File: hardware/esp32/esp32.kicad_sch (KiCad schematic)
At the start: 61 parts, among them J1 Screw_Terminal_01x02, J2 ESP_left, J3 ESP_right, Q4 MMBT5401, Q5 MMBT2222A, U5 LMV321, U6 LM393, U6 LMV321, U8 HT7533-1

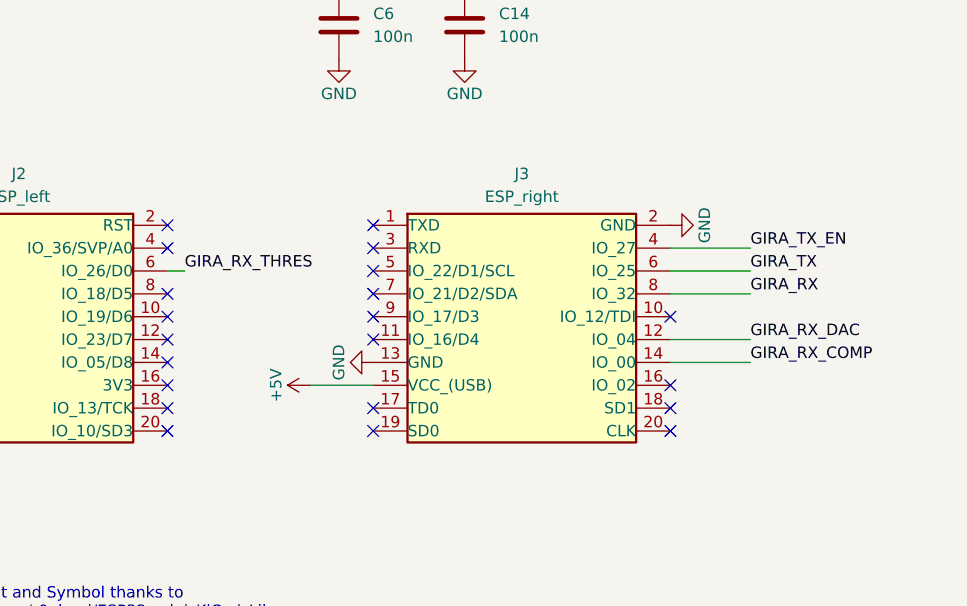
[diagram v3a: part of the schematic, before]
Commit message: Mark boot pins and move rx pins to non boot pins
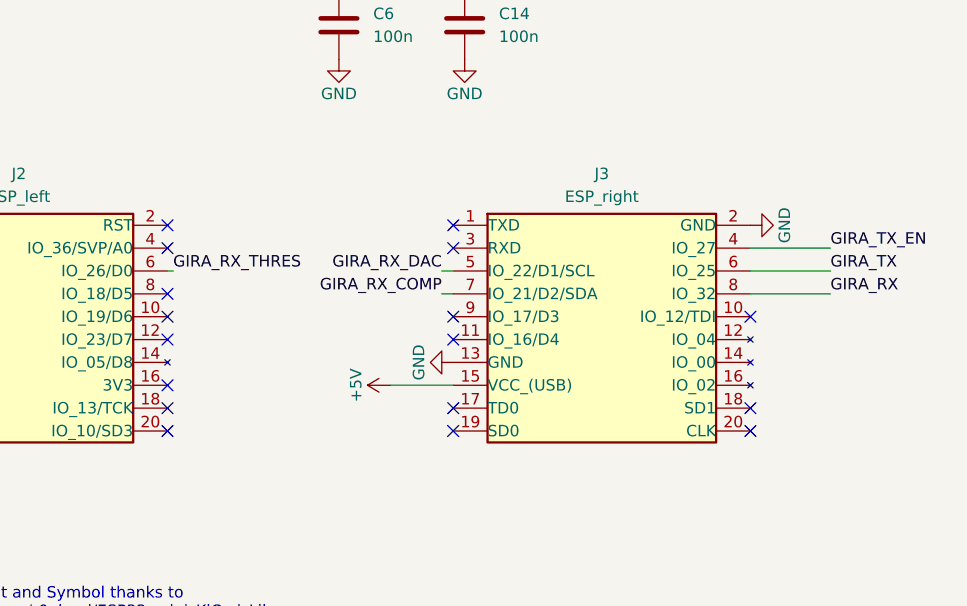
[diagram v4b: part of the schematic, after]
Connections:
- net GIRA_RX_COMP: now also J3.7 (IO_21/D2/SDA); no longer J3.14 (IO_00)
- net GIRA_RX_DAC: now also J3.5 (IO_22/D1/SCL); no longer J3.12 (IO_04)
- no-connect marks 30 -> 26
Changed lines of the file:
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@@
   (no_connect (at 320.04 112.395))
   (no_connect (at 287.02 114.935))
-  (no_connect (at 375.92 117.475))
   (no_connect (at 320.04 109.855))
-  (no_connect (at 342.9 102.235))
+  (no_connect (at 351.79 102.235))
   (no_connect (at 287.02 112.395))
   (no_connect (at 287.02 102.235))
-  (no_connect (at 342.9 122.555))
+  (no_connect (at 351.79 122.555))
   (no_connect (at 287.02 107.315))
   (no_connect (at 287.02 109.855))
@@
   (no_connect (at 320.04 99.695))
   (no_connect (at 320.04 117.475))
-  (no_connect (at 342.9 112.395))
-  (no_connect (at 342.9 109.855))
+  (no_connect (at 351.79 112.395))
+  (no_connect (at 351.79 109.855))
   (no_connect (at 287.02 120.015))
-  (no_connect (at 320.04 114.935))
   (no_connect (at 287.02 122.555))
-  (no_connect (at 342.9 107.315))
-  (no_connect (at 342.9 120.015))
+  (no_connect (at 351.79 120.015))
   (no_connect (at 320.04 122.555))
   (no_connect (at 320.04 120.015))
   (no_connect (at 287.02 104.775))
-  (no_connect (at 375.92 120.015))
-  (no_connect (at 375.92 122.555))
-  (no_connect (at 375.92 109.855))
-  (no_connect (at 342.9 99.695))
+  (no_connect (at 384.81 120.015))
+  (no_connect (at 384.81 122.555))
+  (no_connect (at 384.81 109.855))
+  (no_connect (at 351.79 99.695))
   (no_connect (at 287.02 117.475))
   (no_connect (at 320.04 102.235))
-  (no_connect (at 342.9 104.775))
   (wire (pts (xy 235.585 231.14) (xy 235.585 232.41))
     (stroke (width 0) (type default))
@@
     (stroke (width 0) (type default))
   )
-  (wire (pts (xy 384.81 104.775) (xy 375.92 104.775))
+  (wire (pts (xy 393.7 104.775) (xy 384.81 104.775))
     (stroke (width 0) (type default))
   )
@@
     (stroke (width 0) (type default))
   )
-  (wire (pts (xy 335.915 117.475) (xy 342.9 117.475))
+  (wire (pts (xy 344.805 117.475) (xy 351.79 117.475))
     (stroke (width 0) (type default))
   )
@@
     (stroke (width 0) (type default))
   )
-  (wire (pts (xy 375.92 107.315) (xy 384.81 107.315))
+  (wire (pts (xy 384.81 107.315) (xy 393.7 107.315))
     (stroke (width 0) (type default))
   )
@@
     (stroke (width 0) (type default))
   )
-  (wire (pts (xy 384.81 102.235) (xy 375.92 102.235))
+  (wire (pts (xy 393.7 102.235) (xy 384.81 102.235))
     (stroke (width 0) (type default))
   )
@@
     (stroke (width 0) (type default))
   )
-  (wire (pts (xy 321.945 104.775) (xy 320.04 104.775))
+  (wire (pts (xy 320.675 104.775) (xy 320.04 104.775))
     (stroke (width 0) (type default))
   )
@@
     (stroke (width 0) (type default))
   )
-  (wire (pts (xy 384.81 114.935) (xy 375.92 114.935))
+  (wire (pts (xy 350.52 107.315) (xy 351.79 107.315))
     (stroke (width 0) (type default))
   )
-  (wire (pts (xy 384.81 112.395) (xy 375.92 112.395))
+  (wire (pts (xy 350.52 104.775) (xy 351.79 104.775))
     (stroke (width 0) (type default))
   )
@@
     (effects (font (size 1.27 1.27)) (justify left bottom))
   )
-  (label "GIRA_RX_DAC" (at 384.81 112.395 0) (fields_autoplaced)
-    (effects (font (size 1.27 1.27)) (justify left bottom))
+  (label "GIRA_RX_DAC" (at 350.52 104.775 180) (fields_autoplaced)
+    (effects (font (size 1.27 1.27)) (justify right bottom))
   )
   (label "GIRA_RX" (at 257.81 53.34 0) (fields_autoplaced)
@@
     (effects (font (size 1.27 1.27)) (justify right bottom))
   )
-  (label "GIRA_RX_COMP" (at 384.81 114.935 0) (fields_autoplaced)
-    (effects (font (size 1.27 1.27)) (justify left bottom))
+  (label "GIRA_RX_COMP" (at 350.52 107.315 180) (fields_autoplaced)
+    (effects (font (size 1.27 1.27)) (justify right bottom))
   )
   (label "GIRA_TX_EN" (at 266.065 178.435 180) (fields_autoplaced)
     (effects (font (size 1.27 1.27)) (justify right bottom))
   )
-  (label "GIRA_RX_THRES" (at 321.945 104.775 0) (fields_autoplaced)
+  (label "GIRA_RX_THRES" (at 320.675 104.775 0) (fields_autoplaced)
     (effects (font (size 1.27 1.27)) (justify left bottom))
   )
-  (label "GIRA_RX" (at 384.81 107.315 0) (fields_autoplaced)
+  (label "GIRA_RX" (at 393.7 107.315 0) (fields_autoplaced)
     (effects (font (size 1.27 1.27)) (justify left bottom))
   )
-  (label "GIRA_TX_EN" (at 384.81 102.235 0) (fields_autoplaced)
+  (label "GIRA_TX_EN" (at 393.7 102.235 0) (fields_autoplaced)
     (effects (font (size 1.27 1.27)) (justify left bottom))
   )
-  (label "GIRA_TX" (at 384.81 104.775 0) (fields_autoplaced)
+  (label "GIRA_TX" (at 393.7 104.775 0) (fields_autoplaced)
     (effects (font (size 1.27 1.27)) (justify left bottom))
   )
@@
     )
   )
-  (symbol (lib_id "symbols:GND") (at 342.9 114.935 270) (mirror x) (unit 1)
+  (symbol (lib_id "symbols:GND") (at 351.79 114.935 270) (mirror x) (unit 1)
     (in_bom yes) (on_board yes) (dnp no)
-    (property "Reference" "#PWR0120" (at 336.55 114.935 0)
+    (property "Reference" "#PWR0120" (at 345.44 114.935 0)
       (effects (font (size 1.27 1.27)) hide)
     )
-    (property "Value" "GND" (at 339.09 114.935 0)
+    (property "Value" "GND" (at 347.98 114.935 0)
       (effects (font (size 1.27 1.27)))
     )
-    (property "Footprint" "" (at 342.9 114.935 0)
+    (property "Footprint" "" (at 351.79 114.935 0)
       (effects (font (size 1.27 1.27)) hide)
     )
-    (property "Datasheet" "" (at 342.9 114.935 0)
+    (property "Datasheet" "" (at 351.79 114.935 0)
       (effects (font (size 1.27 1.27)) hide)
     )
@@
     )
   )
-  (symbol (lib_id "symbols:ESP_right") (at 347.98 109.855 0) (unit 1)
+  (symbol (lib_id "symbols:ESP_right") (at 356.87 109.855 0) (unit 1)
     (in_bom yes) (on_board yes) (dnp no) (fields_autoplaced)
-    (property "Reference" "J3" (at 359.41 93.98 0)
+    (property "Reference" "J3" (at 368.3 93.98 0)
       (effects (font (size 1.27 1.27)))
     )
-    (property "Value" "ESP_right" (at 359.41 96.52 0)
+    (property "Value" "ESP_right" (at 368.3 96.52 0)
       (effects (font (size 1.27 1.27)))
     )
-    (property "Footprint" "Library:PinHeader_2x10_P2.54mm_Vertical" (at 349.25 130.175 0)
+    (property "Footprint" "Library:PinHeader_2x10_P2.54mm_Vertical" (at 358.14 130.175 0)
       (effects (font (size 1.27 1.27)) hide)
     )
-    (property "Datasheet" "~" (at 347.98 109.855 0)
+    (property "Datasheet" "~" (at 356.87 109.855 0)
       (effects (font (size 1.27 1.27)) hide)
     )
-    (property "MPN" "C7501280" (at 334.01 128.905 0)
+    (property "MPN" "C7501280" (at 342.9 128.905 0)
       (effects (font (size 1.27 1.27)) hide)
     )
-    (property "JlcRotOffset" "-90" (at 347.98 109.855 0)
+    (property "JlcRotOffset" "-90" (at 356.87 109.855 0)
       (effects (font (size 1.27 1.27)) hide)
     )
-    (property "JlcPosOffset" "11.43,1.27" (at 347.98 109.855 0)
+    (property "JlcPosOffset" "11.43,1.27" (at 356.87 109.855 0)
       (effects (font (size 1.27 1.27)) hide)
     )
@@
     )
   )
-  (symbol (lib_id "symbols:GND") (at 375.92 99.695 90) (mirror x) (unit 1)
+  (symbol (lib_id "symbols:GND") (at 384.81 99.695 90) (mirror x) (unit 1)
     (in_bom yes) (on_board yes) (dnp no)
-    (property "Reference" "#PWR0120" (at 382.27 99.695 0)
+    (property "Reference" "#PWR0120" (at 391.16 99.695 0)
       (effects (font (size 1.27 1.27)) hide)
     )
-    (property "Value" "GND" (at 379.73 99.695 0)
+    (property "Value" "GND" (at 388.62 99.695 0)
       (effects (font (size 1.27 1.27)))
     )
-    (property "Footprint" "" (at 375.92 99.695 0)
+    (property "Footprint" "" (at 384.81 99.695 0)
       (effects (font (size 1.27 1.27)) hide)
     )
-    (property "Datasheet" "" (at 375.92 99.695 0)
+    (property "Datasheet" "" (at 384.81 99.695 0)
       (effects (font (size 1.27 1.27)) hide)
     )
@@
     )
   )
-  (symbol (lib_id "symbols:+5V") (at 335.915 117.475 90) (unit 1)
+  (symbol (lib_id "symbols:+5V") (at 344.805 117.475 90) (unit 1)
     (in_bom yes) (on_board yes) (dnp no)
-    (property "Reference" "#PWR0178" (at 339.725 117.475 0)
+    (property "Reference" "#PWR0178" (at 348.615 117.475 0)
       (effects (font (size 1.27 1.27)) hide)
     )
-    (property "Value" "+5V" (at 332.105 117.475 0)
+    (property "Value" "+5V" (at 340.995 117.475 0)
       (effects (font (size 1.27 1.27)))
     )
-    (property "Footprint" "" (at 335.915 117.475 0)
+    (property "Footprint" "" (at 344.805 117.475 0)
       (effects (font (size 1.27 1.27)) hide)
     )
-    (property "Datasheet" "" (at 335.915 117.475 0)
+    (property "Datasheet" "" (at 344.805 117.475 0)
       (effects (font (size 1.27 1.27)) hide)
     )

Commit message: Working on V3.1
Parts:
- removed R22 (x2): 47k, Library:R_0603_1608Metric_Pad0.98x0.95mm_HandSolder, symbol symbols:47k
- removed R23: 10k, Library:R_0603_1608Metric_Pad0.98x0.95mm_HandSolder, symbol symbols:10k
- removed R35: 2k4, Library:R_0603_1608Metric_Pad0.98x0.95mm_HandSolder, symbol symbols:2k4
- removed R45: 4k7, Library:R_0603_1608Metric_Pad0.98x0.95mm_HandSolder, symbol symbols:4k7
- added C17: 100p, Library:C_0603_1608Metric_Pad1.08x0.95mm_HandSolder, symbol symbols:100p
- added R14: 1k, Library:R_0603_1608Metric_Pad0.98x0.95mm_HandSolder, symbol symbols:1k
- added R2: 22k, Library:R_0603_1608Metric_Pad0.98x0.95mm_HandSolder, symbol symbols:22k
- added R34 (x2): 18k, Library:R_0603_1608Metric_Pad0.98x0.95mm_HandSolder, symbol symbols:18k
- added R34: 0, Library:R_0603_1608Metric_Pad0.98x0.95mm_HandSolder, symbol symbols:0R
- C19: now not fitted
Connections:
- net +5V: no longer C14.1, R39.1, R40.2, U5.5 (V+)
- net GND: now also C17.1, R34.1
- net at C19.2, R43.1, R45.2: now also R34.1
- net 5V_onoff: now reaches C21.1, Q4.3 (C1), U.5 (V+)
- net 5V_onoff: now also C14.1, R39.1, R40.2, U5.5 (V+), R34.1
- net at U.3 (-): now also R2.2, R34.2, R34.2
- net at R38.2, R39.2, U5.3 (-): now also R14.2
- net at R28.1, R34.1, U5.4: now also R14.1
- net at R28.2, U.1 (+): now also C17.2
- net at C4.1, U.4: now also R2.1
- net GIRA_RX renamed RX_ANA
- net GIRA_RX_COMP renamed RX
- net GIRA_RX_DAC renamed RX_DAC
- net GIRA_RX_THRES renamed DAC_OUT
- net GIRA_TX renamed TX
- net TX: now also R34.2
- net GIRA_TX_EN renamed TX_EN
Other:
- moved on the sheet: C14, U6C

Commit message: Add logo
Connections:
- net DAC_OUT renamed RX_THRESH
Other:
- title: (none) -> ESP32 Mini

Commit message: Work on V3.1
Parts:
- C17: now not fitted
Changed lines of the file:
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@@
   )
   (symbol (lib_id "symbols:100p") (at 143.51 222.25 0) (mirror x) (unit 1)
-    (in_bom yes) (on_board yes) (dnp no)
+    (in_bom yes) (on_board yes) (dnp yes)
     (property "Reference" "C17" (at 147.32 220.345 0)
       (effects (font (size 1.27 1.27)) (justify right))

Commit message: Work on V3.1
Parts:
- removed U8: HT7533-1, Library:SOT-89-3, symbol symbols:HT7533-1
- added D2: SS14, Library:D_SMA, symbol symbols:SS14
- added J4: PlugIn_Terminal_01x02, Library:steckklemme2x1_dnp, symbol symbols:PlugIn_Terminal_01x02_dnp
- added J5: Plugged into C8387, Library:nofoorprint, symbol symbols:PlugIn Stecker
- added S1: SYM_ESD_Small, Library:ESD-Logo_6.6x6mm_SilkScreen, symbol symbols:SYM_ESD_Small
- added U4: ~, Library:ESP32_mini_no_pads, symbol symbols:ESPSilkscreen
- C14, C16, C24, C31, C6: footprint Library:C_0603_1608Metric_Pad1.08x0.95mm_HandSolder -> Library:C_0402_1005Metric_Pad0.74x0.62mm_HandSolder; symbol symbols:100n -> symbols:100n_0402; MPN C14663 -> C307331
- C21: value 10n -> 100n; footprint Library:C_0603_1608Metric_Pad1.08x0.95mm_HandSolder -> Library:C_0402_1005Metric_Pad0.74x0.62mm_HandSolder; symbol symbols:10n -> symbols:100n_0402; MPN C57112 -> C307331
- J1: value Screw_Terminal_01x02 -> PlugIn_Terminal_01x02; footprint Library:anschlussklemme2x1 -> Library:steckklemme2x1_1; symbol symbols:Screw_Terminal_01x02 -> symbols:PlugIn_Terminal_01x02_1; JlcRotOffset (none) -> -180; MPN C8385 -> C8387
- R25: footprint Library:R_0603_1608Metric_Pad0.98x0.95mm_HandSolder -> Library:R_0402_1005Metric_Pad0.72x0.64mm_HandSolder; symbol symbols:10k -> symbols:10k_0402; MPN C25804 -> C25744
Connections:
- net +3.3V: now also J2.16 (3V3)
- net +5V: now also D2.1 (K)
- net GND: now also J4.1 (Pin_1)
- net at D1.3: now also J1.2 (Pin_2); no longer J1.1 (Pin_1)
- net at D1.4: now also J1.1 (Pin_1); no longer J1.2 (Pin_2)
- new net: D2.2 (A), J4.2 (Pin_2)
- no-connect marks 26 -> 25
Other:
- note added: "ESP32mini has Schottky on its 5V output"
- note added: "https://www.phoenixcontact.com/de-de/produkte/leiterplattenstecker-mc-15-2-st-381-1803578"
- moved on the sheet: J1
